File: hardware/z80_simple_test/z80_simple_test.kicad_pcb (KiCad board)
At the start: 2 copper layers, 95 x 100 mm, 49 parts, among them J2 Conn_02x15_Odd_Even, J3 Conn_01x32, U1 Z84C000XPEG, U2 SRAM_512K8B_DIP_SOP_SOJ, U3 EEPROM_512K8B_DIP, U4 74XX138, U5 74XX273, U6 74XX32, U7 74XX00, U8 74XX32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

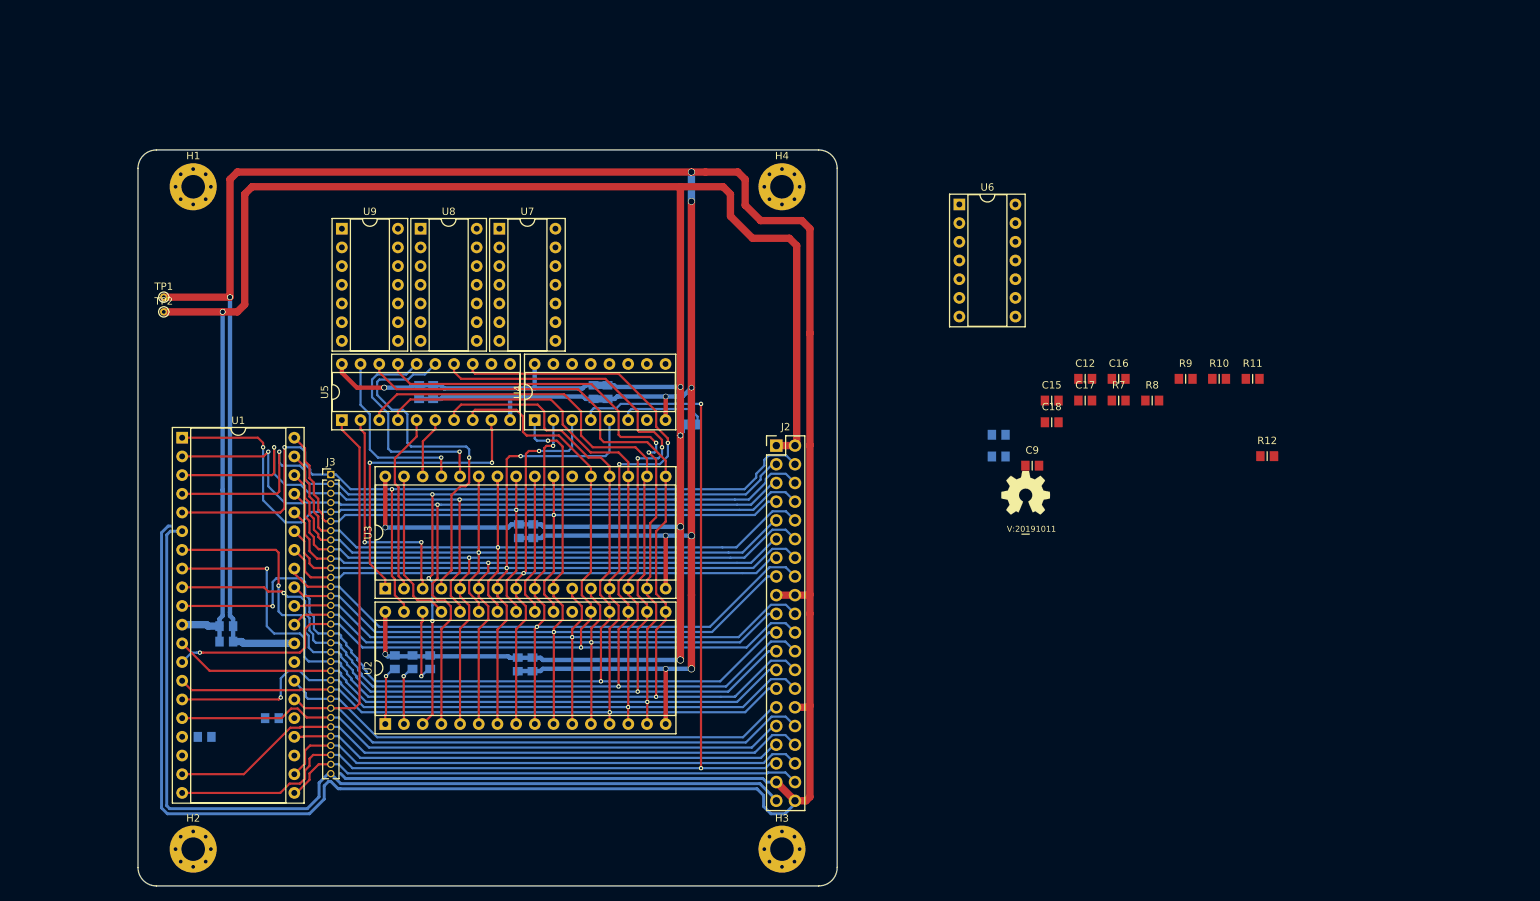
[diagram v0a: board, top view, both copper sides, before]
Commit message: relayout of busses, more compactified, added two PIO's to check space for SIO
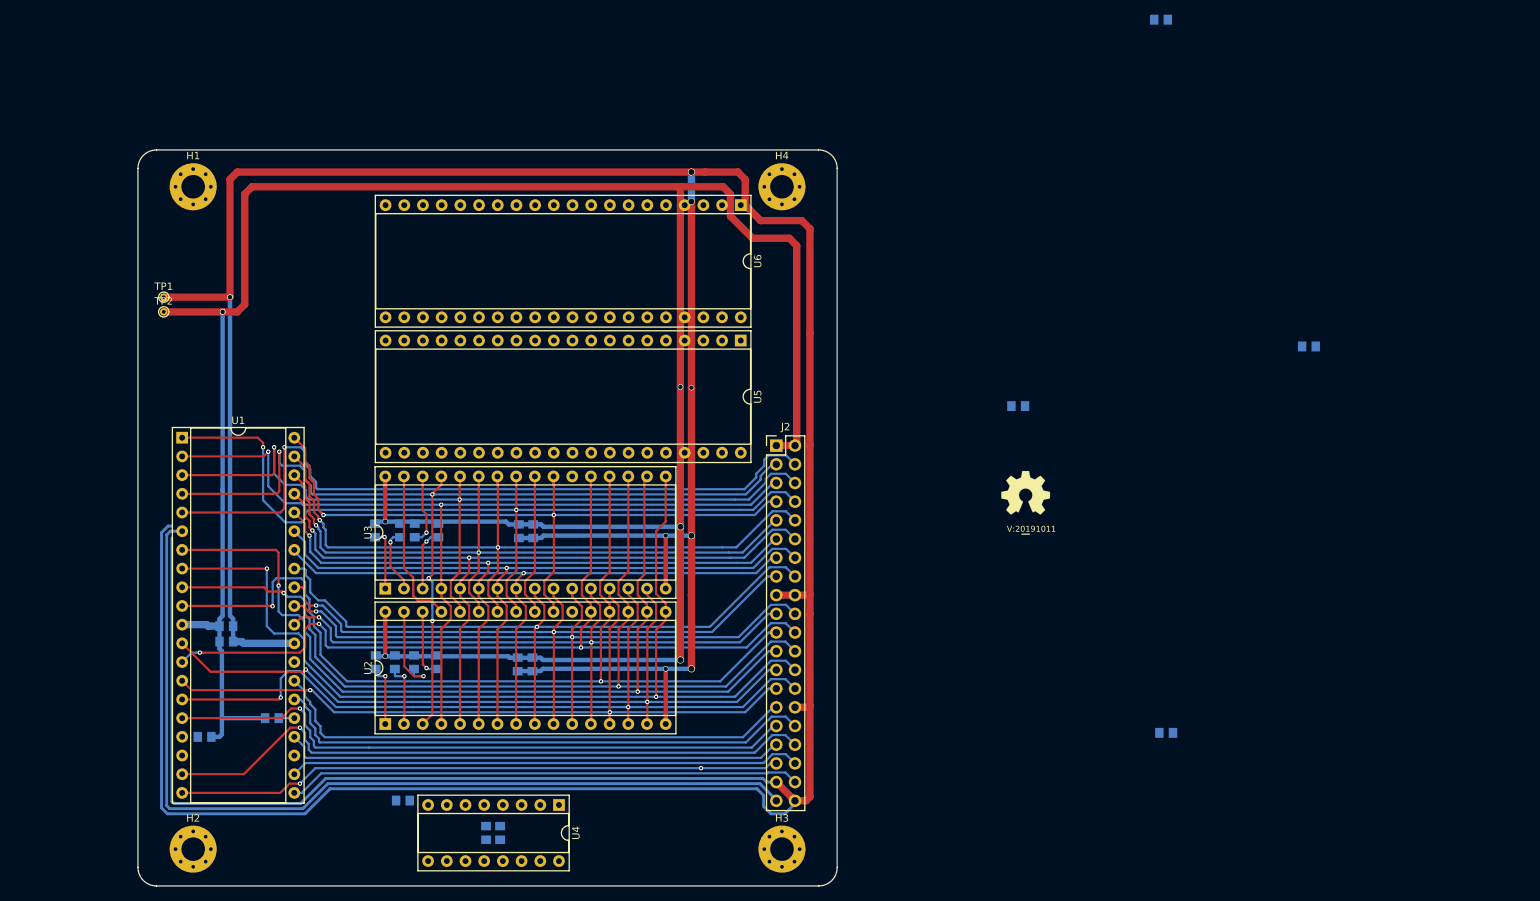
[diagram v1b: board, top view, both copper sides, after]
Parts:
- removed C13, C15, C17: 100n, SquantorRcl:C_0805+0603
- removed C14, C16, C18: 1u, SquantorRcl:C_0805+0603
- removed J3: Conn_01x32, Connector_PinHeader_1.27mm:PinHeader_1x33_P1.27mm_Vertical
- removed R12: 10k, SquantorRcl:C_0805+0603
- removed U7, U9: 74XX00, Package_DIP:DIP-14_W7.62mm_Socket
- removed U8: 74XX32, Package_DIP:DIP-14_W7.62mm_Socket
- C12, C9, R10, R11, R7, R8, R9: moved to B.Cu
- U5: value 74XX273 -> Z84C200XPEG; footprint Package_DIP:DIP-20_W7.62mm_Socket -> Package_DIP:DIP-40_W15.24mm_Socket
- U6: value 74XX32 -> Z84C200XPEG; footprint Package_DIP:DIP-14_W7.62mm_Socket -> Package_DIP:DIP-40_W15.24mm_Socket
- moved R11 121.0 mm to (134.7, 101.7), turned to 90 degrees
- moved C10 112.8 mm to (241.5, 32.3), turned to 0 degrees
- moved R10 111.2 mm to (140.1, 101.7), turned to 90 degrees
- moved C11 109.8 mm to (242.2, 129.2), turned to 0 degrees
- moved R9 108.7 mm to (138.1, 101.7), turned to 90 degrees
- moved R7 102.1 mm to (140.0, 119.6), turned to 270 degrees
- moved R8 98.6 mm to (143.3, 101.7), turned to 90 degrees
- moved R2 64.3 mm to (138.5, 138.4), turned to 0 degrees
- moved C7 62.1 mm to (149.8, 142.8), turned to 270 degrees
- moved C8 61.2 mm to (151.7, 142.8), turned to 270 degrees
- moved U5 55.3 mm to (184.4, 75.9), turned to 270 degrees
- moved U4 52.4 mm to (159.7, 139.0), turned to 270 degrees
- moved C12 30.7 mm to (261.6, 76.7)
- moved U6 29.7 mm to (184.4, 57.5), turned to 270 degrees
- moved C9 8.32 mm to (222.1, 84.8)
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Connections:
- R10 pad 1: /VDD -> /A17_ROM
- R10 pad 2: Net-(R10-Pad2) -> /VDD
- R11 pad 1: /VDD -> /A18_ROM
- R11 pad 2: Net-(R11-Pad2) -> /VDD
- R7 pad 2: Net-(R7-Pad2) -> /A15_RAM
- R8 pad 1: /VDD -> /A15_ROM
- R8 pad 2: Net-(R8-Pad2) -> /VDD
- R9 pad 1: /VDD -> /A16_ROM
- R9 pad 2: Net-(R9-Pad2) -> /VDD
- U2 pad 22: /!RAM_CE -> (no net)
- U2 pad 31: /A15 -> /A15_RAM
- U3 pad 22: /!ROM_CE -> (no net)
- U3 pad 28: /A13_ROM -> /A13
- U3 pad 29: /A14_ROM -> /A14
- U3 pad 4: /A12_ROM -> /A12
- U4 pad 15: /!IOSEL0 -> (no net)
- U5 pad 1: /!RESET -> /D2
- U5 pad 10: /VSS -> (no net)
- U5 pad 11: /BANK_CP -> /VSS
- U5 pad 12: /!BOOT -> (no net)
- U5 pad 13: /D0 -> (no net)
- U5 pad 14: /D1 -> (no net)
- U5 pad 15: /A12_ROM -> (no net)
- U5 pad 16: /A13_ROM -> (no net)
- U5 pad 17: /D2 -> (no net)
- U5 pad 18: /D3 -> (no net)
- U5 pad 19: /A14_ROM -> /D0
- U5 pad 2: /A15_ROM -> /D7
- U5 pad 20: /VDD -> /D1
- U5 pad 3: /D4 -> /D6
- U5 pad 4: /D5 -> /SEL_PIO
- U5 pad 5: /A16_ROM -> /A1
- U5 pad 6: /A17_ROM -> /A0
- U5 pad 7: /D6 -> (no net)
- U5 pad 8: /D7 -> (no net)
- U5 pad 9: /A18_ROM -> (no net)
- U6 pad 1: /!RD -> /D2
- U6 pad 10: /!IO_WR -> (no net)
- U6 pad 11: /!IO_WR -> /VSS
- U6 pad 12: /!IORQ -> (no net)
- U6 pad 13: /!WR -> (no net)
- U6 pad 14: /VDD -> (no net)
- U6 pad 2: /!MREQ -> /D7
- U6 pad 3: /!MEM_RD -> /D6
- U6 pad 4: /!MREQ -> /SEL_PIO
- U6 pad 5: /!WR -> /A1
- U6 pad 6: /!MEM_WR -> /A0
- U6 pad 7: /VSS -> (no net)
- U6 pad 8: /BANK_CP -> (no net)
- U6 pad 9: /!IOSEL0 -> (no net)
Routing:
- net /!IORQ: track 151.2 -> 82.4 mm
- net /D2: track 169.2 -> 105.5 mm, vias 3 -> 2
- net /D0: track 162.8 -> 103.3 mm, vias 3 -> 2
- net /D1: track 168.5 -> 110.0 mm, vias 4 -> 2
- net /D3: track 180.5 -> 130.9 mm
- net /A12_ROM: track 49.4 -> 0.00 mm, vias 1 -> 0
- net /D4: track 175.4 -> 129.1 mm
- net /!RESET: track 116.1 -> 74.3 mm
- net /D5: track 165.0 -> 125.7 mm
- net /A5: track 129.4 -> 95.5 mm, vias 2 -> 1
- net /A18_ROM: track 40.4 -> 8.35 mm, vias 2 -> 1
- net /VDD: track 398.3 -> 367.2 mm, vias 8 -> 6
- net /A13_ROM: track 30.5 -> 0.00 mm, vias 1 -> 0
- net /D6: track 155.0 -> 126.8 mm
- net /A4: track 117.7 -> 89.8 mm, vias 2 -> 1
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
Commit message: minor layout changes
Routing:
- net /D7: track 116.1 -> 115.2 mm
- net /A0: track 89.3 -> 88.6 mm
- net /A1: track 92.4 -> 91.8 mm

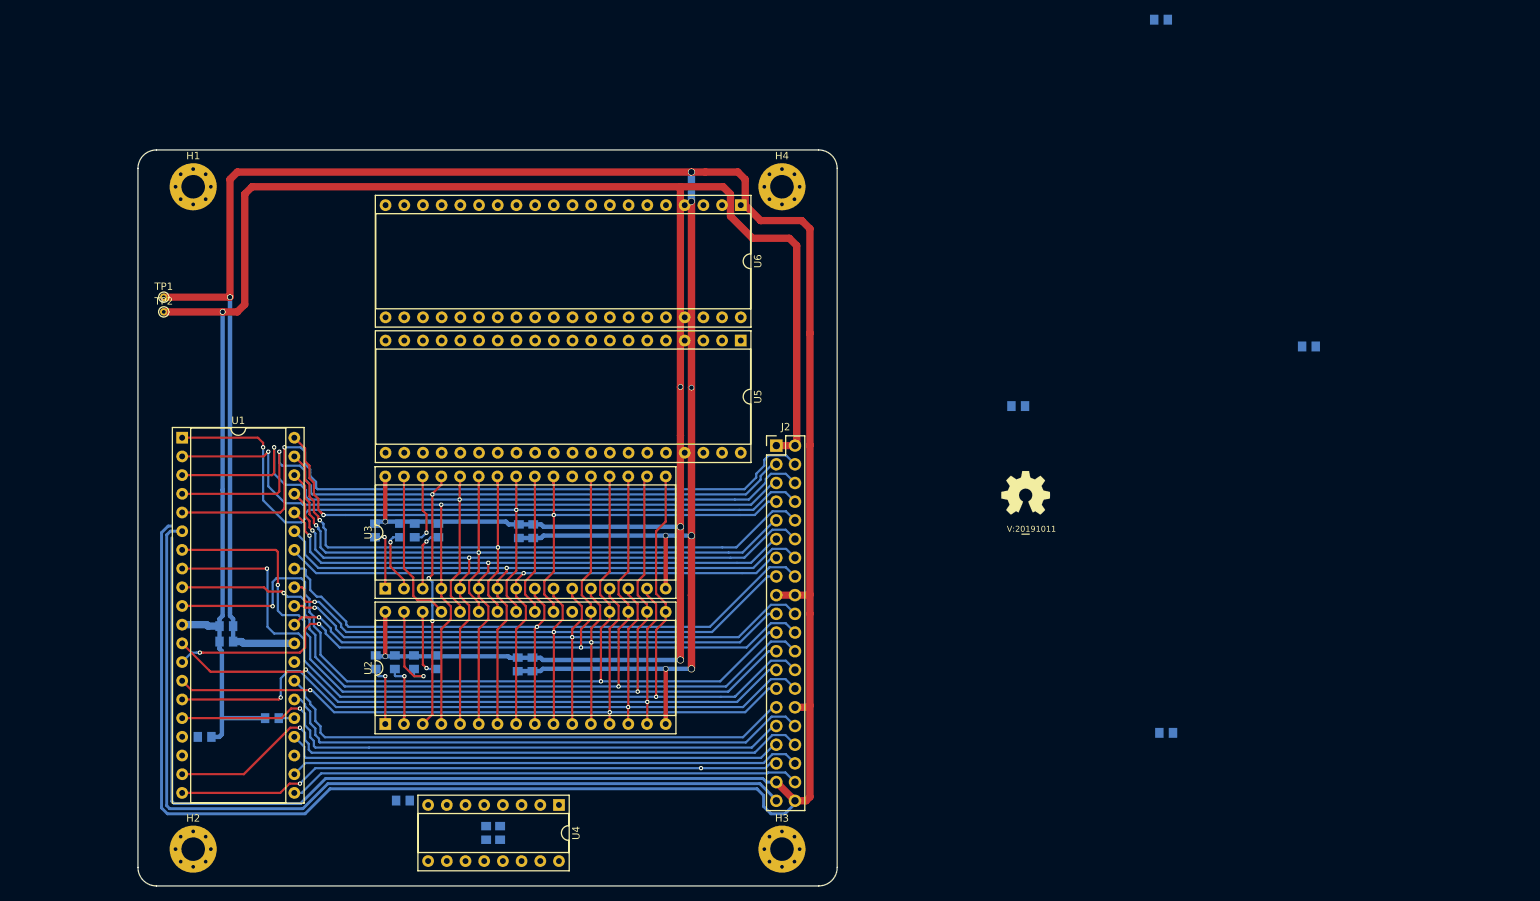
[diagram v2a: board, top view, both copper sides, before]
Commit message: ripped up full bus, now experimenting with different ordering
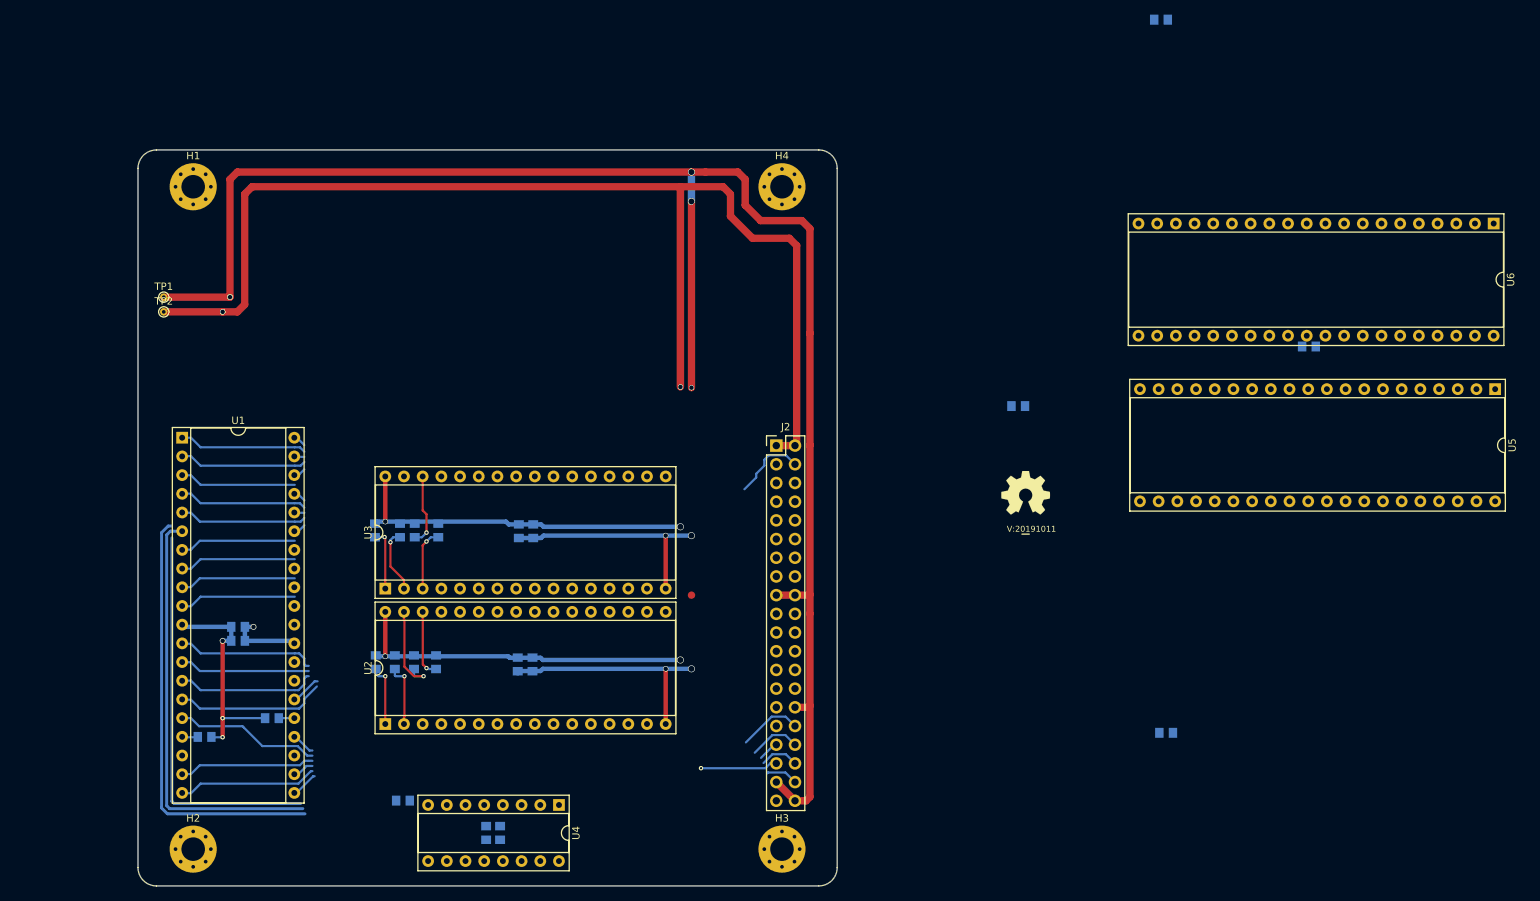
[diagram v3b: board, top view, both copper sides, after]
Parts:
- moved U5 102.7 mm to (286.9, 82.5)
- moved U6 102.3 mm to (286.7, 60.0)
- moved C1 1.60 mm to (116.1, 114.8)
- moved C2 1.60 mm to (116.1, 116.7)
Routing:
- net /VSS: track 634.2 -> 413.5 mm, vias 8 -> 9
- net /D3: track 130.9 -> 15.8 mm, vias 2 -> 0
- net /D4: track 129.1 -> 15.8 mm, vias 2 -> 0
- net /D6: track 126.8 -> 15.9 mm, vias 2 -> 0
- net /A14: track 127.9 -> 17.4 mm, vias 4 -> 0
- net /D5: track 125.7 -> 15.8 mm, vias 2 -> 0
- net /A12: track 118.8 -> 17.4 mm, vias 2 -> 0
- net /A7: track 100.6 -> 1.72 mm, vias 2 -> 0
- net /A9: track 99.7 -> 1.38 mm, vias 2 -> 0
- net /A13: track 114.2 -> 15.8 mm, vias 2 -> 0
- net /D7: track 115.2 -> 17.7 mm, vias 3 -> 0
- net /A11: track 114.7 -> 17.4 mm, vias 2 -> 0
- net /A3: track 96.1 -> 0.00 mm, vias 1 -> 0
- net /A5: track 95.5 -> 1.69 mm, vias 1 -> 0
- net /A6: track 95.0 -> 1.38 mm, vias 2 -> 0
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
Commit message: z84C00 layout side completed, routing bus underneath memory chips
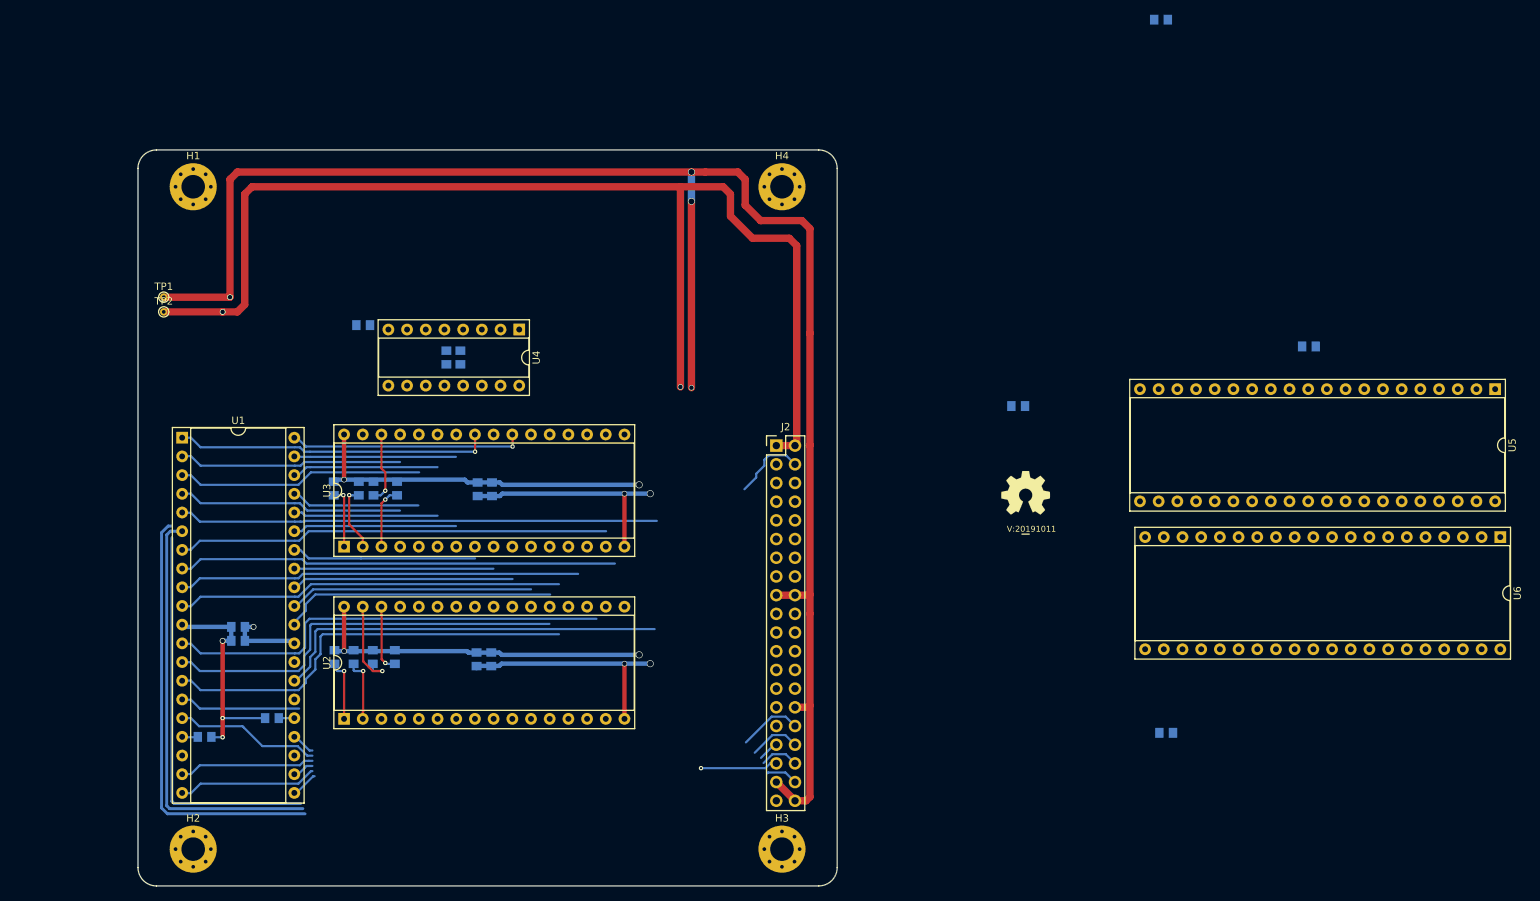
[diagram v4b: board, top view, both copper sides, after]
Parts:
- moved C7 64.8 mm to (144.4, 78.2)
- moved C8 64.8 mm to (146.3, 78.2)
- moved R2 64.8 mm to (133.1, 73.8)
- moved U4 64.8 mm to (154.3, 74.4)
- moved U6 42.6 mm to (287.6, 102.6)
- moved R8 7.99 mm to (137.7, 96.0)
- moved C5 7.99 mm to (150.6, 96.1)
- moved C6 7.99 mm to (148.7, 96.1)
- moved R10 7.99 mm to (134.5, 96.0)
- moved R11 7.99 mm to (129.1, 96.0)
- moved R9 7.99 mm to (132.5, 96.0)
- moved U3 7.99 mm to (130.5, 103.9)
- moved R5 5.64 mm to (129.2, 118.9)
- moved C3 5.64 mm to (148.5, 119.2)
- moved C4 5.64 mm to (150.5, 119.2)
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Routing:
- net /!M1: track 0.00 -> 54.3 mm
- net /A15: track 27.4 -> 75.1 mm
- net /D3: track 15.8 -> 59.6 mm
- net /D4: track 15.8 -> 58.7 mm
- net /D2: track 18.9 -> 60.7 mm
- net /D5: track 15.8 -> 54.6 mm
- net /D0: track 19.0 -> 57.4 mm
- net /D7: track 17.7 -> 55.8 mm
- net /A0: track 0.00 -> 37.2 mm
- net /D6: track 15.9 -> 52.5 mm
- net /A1: track 0.00 -> 33.1 mm
- net /A2: track 0.00 -> 30.1 mm
- net /A10: track 1.77 -> 31.8 mm, vias 0 -> 1
- net /A3: track 0.00 -> 27.1 mm
- net /A11: track 17.4 -> 42.9 mm, vias 0 -> 1
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
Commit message: further layout
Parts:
- moved U6 112.6 mm to (178.7, 131.1)
- moved U5 109.6 mm to (178.8, 64.6)
- moved R2 83.0 mm to (215.4, 63.1)
- moved C7 83.0 mm to (226.7, 67.5)
- moved C8 83.0 mm to (228.6, 67.5)
- moved U4 83.0 mm to (236.6, 63.7)
- moved R4 0.40 mm to (131.8, 119.3)
- moved R5 0.38 mm to (129.2, 119.3)
- moved R6 0.38 mm to (137.4, 119.3)
- moved R7 0.38 mm to (134.4, 119.3)
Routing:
- net /D1: track 16.4 -> 96.0 mm, vias 0 -> 1
- net /!RESET: track 8.65 -> 64.0 mm
- net /!MREQ: track 25.5 -> 78.3 mm
- net /!WAIT: track 6.05 -> 56.7 mm
- net /!INT: track 19.8 -> 69.6 mm
- net /A12: track 30.4 -> 77.3 mm, vias 0 -> 1
- net /A14: track 30.6 -> 76.3 mm, vias 0 -> 1
- net /A1: track 33.1 -> 74.7 mm, vias 0 -> 1
- net /D7: track 55.8 -> 95.4 mm, vias 0 -> 1
- net /A0: track 37.2 -> 76.1 mm, vias 0 -> 1
- net /D0: track 57.4 -> 95.4 mm, vias 0 -> 1
- net /A7: track 17.5 -> 55.5 mm, vias 0 -> 1
- net /D6: track 52.5 -> 90.2 mm, vias 0 -> 1
- net /A13: track 33.5 -> 70.9 mm, vias 0 -> 1
- net /D5: track 54.6 -> 89.7 mm, vias 0 -> 1
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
